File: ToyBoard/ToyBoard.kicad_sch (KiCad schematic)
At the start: 18 parts, among them J5 MSD-1-A, Q1 NMOS, Q2 NMOS

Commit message: Pcb and Gerbs for JLCPCB
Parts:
- removed LM66200DRLR1: ~, Package_TO_SOT_SMD:SOT-583-8, symbol NotinKi:LM66200DRLR
- added C2: C, Capacitor_SMD:C_0402_1005Metric_Pad0.74x0.62mm_HandSolder, symbol Device:C
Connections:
- net COVER_GND: now also C2.2
- net at C1.1, J5.4 (VDD), R1.1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: now also C2.1; no longer J5.3 (CMD), XiaoNRF1.5 (MISO)
- new net: J5.3 (CMD), XiaoNRF1.5 (MISO)
- no-connect marks 18 -> 15
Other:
- moved on the sheet: R1

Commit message: wiring rework
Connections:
- net at C1.1, C2.1, J5.4 (VDD)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: now also R1.2; no longer R1.1
- net at J5.2 (CD/DAT3), XiaoNRF1.4 (CS): now also R1.1; no longer R1.2
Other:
- moved on the sheet: R1
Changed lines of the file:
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@@
-	)
-	(junction
-		(at 134.62 135.89)
-		(diameter 0)
-		(color 0 0 0 0)
 	)
 	(junction
@@
 		(color 0 0 0 0)
 	)
+	(junction
+		(at 128.27 135.89)
+		(diameter 0)
+		(color 0 0 0 0)
+	)
 	(no_connect
 		(at 133.35 102.87)
@@
 	(wire
 		(pts
-			(xy 125.73 142.24) (xy 125.73 153.67)
+			(xy 125.73 142.24) (xy 125.73 143.51)
 		)
 		(stroke
@@
 	(wire
 		(pts
-			(xy 125.73 153.67) (xy 127 153.67)
+			(xy 128.27 135.89) (xy 148.59 135.89)
 		)
 		(stroke
@@
 	(wire
 		(pts
-			(xy 134.62 135.89) (xy 148.59 135.89)
-		)
-		(stroke
-			(width 0)
-			(type default)
-		)
-	)
-	(wire
-		(pts
 			(xy 127 87.63) (xy 125.73 87.63)
 		)
@@
 	(wire
 		(pts
+			(xy 128.27 151.13) (xy 128.27 135.89)
+		)
+		(stroke
+			(width 0)
+			(type default)
+		)
+	)
+	(wire
+		(pts
+			(xy 125.73 151.13) (xy 128.27 151.13)
+		)
+		(stroke
+			(width 0)
+			(type default)
+		)
+	)
+	(wire
+		(pts
 			(xy 109.22 69.85) (xy 96.52 69.85)
 		)
@@
 	(wire
 		(pts
-			(xy 128.27 135.89) (xy 134.62 135.89)
-		)
-		(stroke
-			(width 0)
-			(type default)
-		)
-	)
-	(wire
-		(pts
 			(xy 77.47 60.96) (xy 76.2 60.96)
 		)
@@
 		(pts
 			(xy 125.73 142.24) (xy 125.73 133.35)
-		)
-		(stroke
-			(width 0)
-			(type default)
-		)
-	)
-	(wire
-		(pts
-			(xy 134.62 135.89) (xy 134.62 153.67)
 		)
 		(stroke
@@
 		(on_board yes)
 		(dnp no)
-		(fields_autoplaced yes)
 		(property "Reference" "MAX98357"
-			(at 111.76 144.7799 90)
+			(at 88.646 140.97 0)
 			(effects
 				(font
@@
 		)
 		(property "Value" "~"
-			(at 111.76 147.3199 90)
+			(at 86.614 146.05 0)
 			(effects
 				(font
@@
 	(symbol
 		(lib_id "Device:R")
-		(at 130.81 153.67 270)
+		(at 125.73 147.32 0)
 		(unit 1)
 		(exclude_from_sim no)
@@
 		(dnp no)
 		(property "Reference" "R1"
-			(at 127 155.448 90)
+			(at 128.016 147.32 90)
 			(effects
 				(font
@@
 		)
 		(property "Value" "10k"
-			(at 129.794 156.464 90)
+			(at 123.444 147.32 90)
 			(effects
 				(font
@@
 		)
 		(property "Footprint" "Resistor_SMD:R_0805_2012Metric_Pad1.20x1.40mm_HandSolder"
-			(at 130.81 151.892 90)
+			(at 123.952 147.32 90)
 			(effects
 				(font
@@
 		)
 		(property "Datasheet" "~"
-			(at 130.81 153.67 0)
+			(at 125.73 147.32 0)
 			(effects
 				(font
@@
 		)
 		(property "Description" "Resistor"
-			(at 130.81 153.67 0)
-			(effects
-				(font
+			(at 125.73 147.32 0)
+			(effects
+				(font

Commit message: cleared schem
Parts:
- renumbered U1 to LiPo_charger1
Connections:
- net pwm_out1: now reaches Q1.2 (G), R3.1, XiaoNRF1.8 (PWM1)
- net pwm_out2: now reaches Q2.2 (G), R4.1, XiaoNRF1.10 (PWM2)
- net max_din: now reaches MAX98357.5 (DIN), XiaoNRF1.11 (D4)
- net max_bclk: now reaches MAX98357.6 (BCLK), XiaoNRF1.12 (D5)
- net max_lrc: now reaches MAX98357.7 (LRC), XiaoNRF1.13 (D6)
- net 3V3: now reaches C1.1, C2.1, J5.4 (VDD), R1.2, XiaoNRF1.3 (3V3)
- net sd_cs: now reaches J5.2 (CD/DAT3), R1.1, XiaoNRF1.4 (CS)
- net sd_mosi: now reaches J5.3 (CMD), XiaoNRF1.5 (MOSI)
- net sd_sck: now reaches J5.5 (CLK), XiaoNRF1.6 (SCK)
- net sd_miso: now reaches J5.7 (DAT0), XiaoNRF1.7 (MISO)
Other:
- moved on the sheet: C1, C2, D1, D2, D3, J1, J2, J3, MAX98357, Q1, Q2, R3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

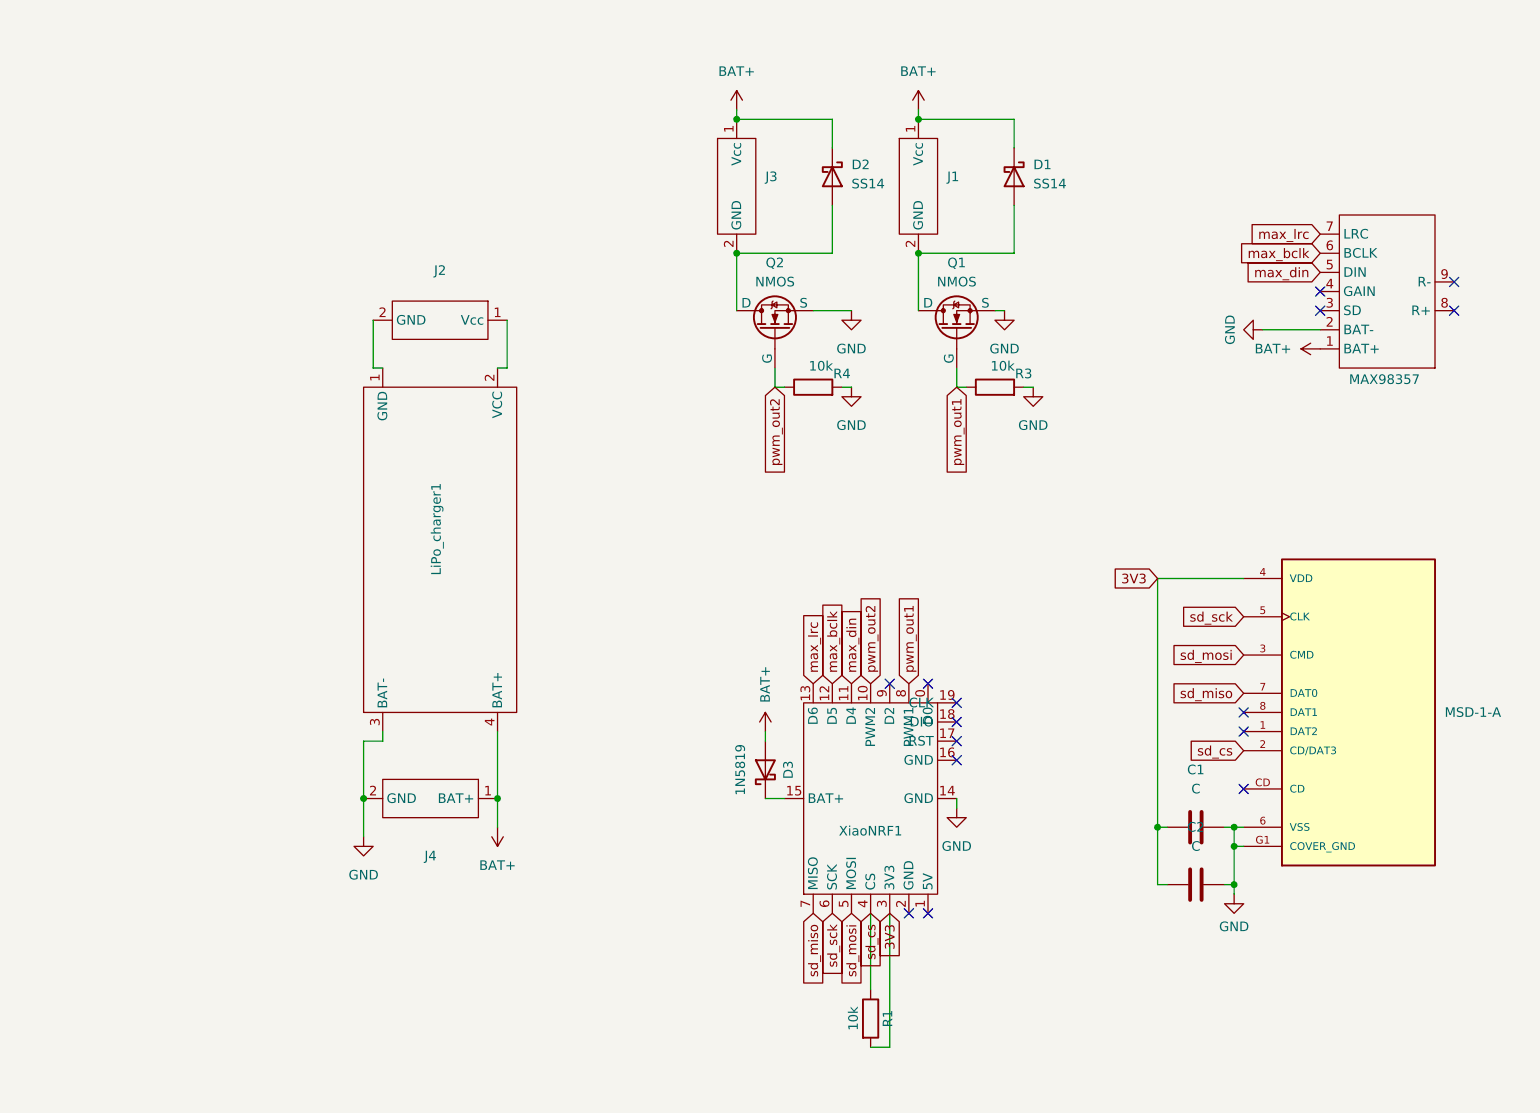
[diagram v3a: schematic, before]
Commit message: cleaner schematic
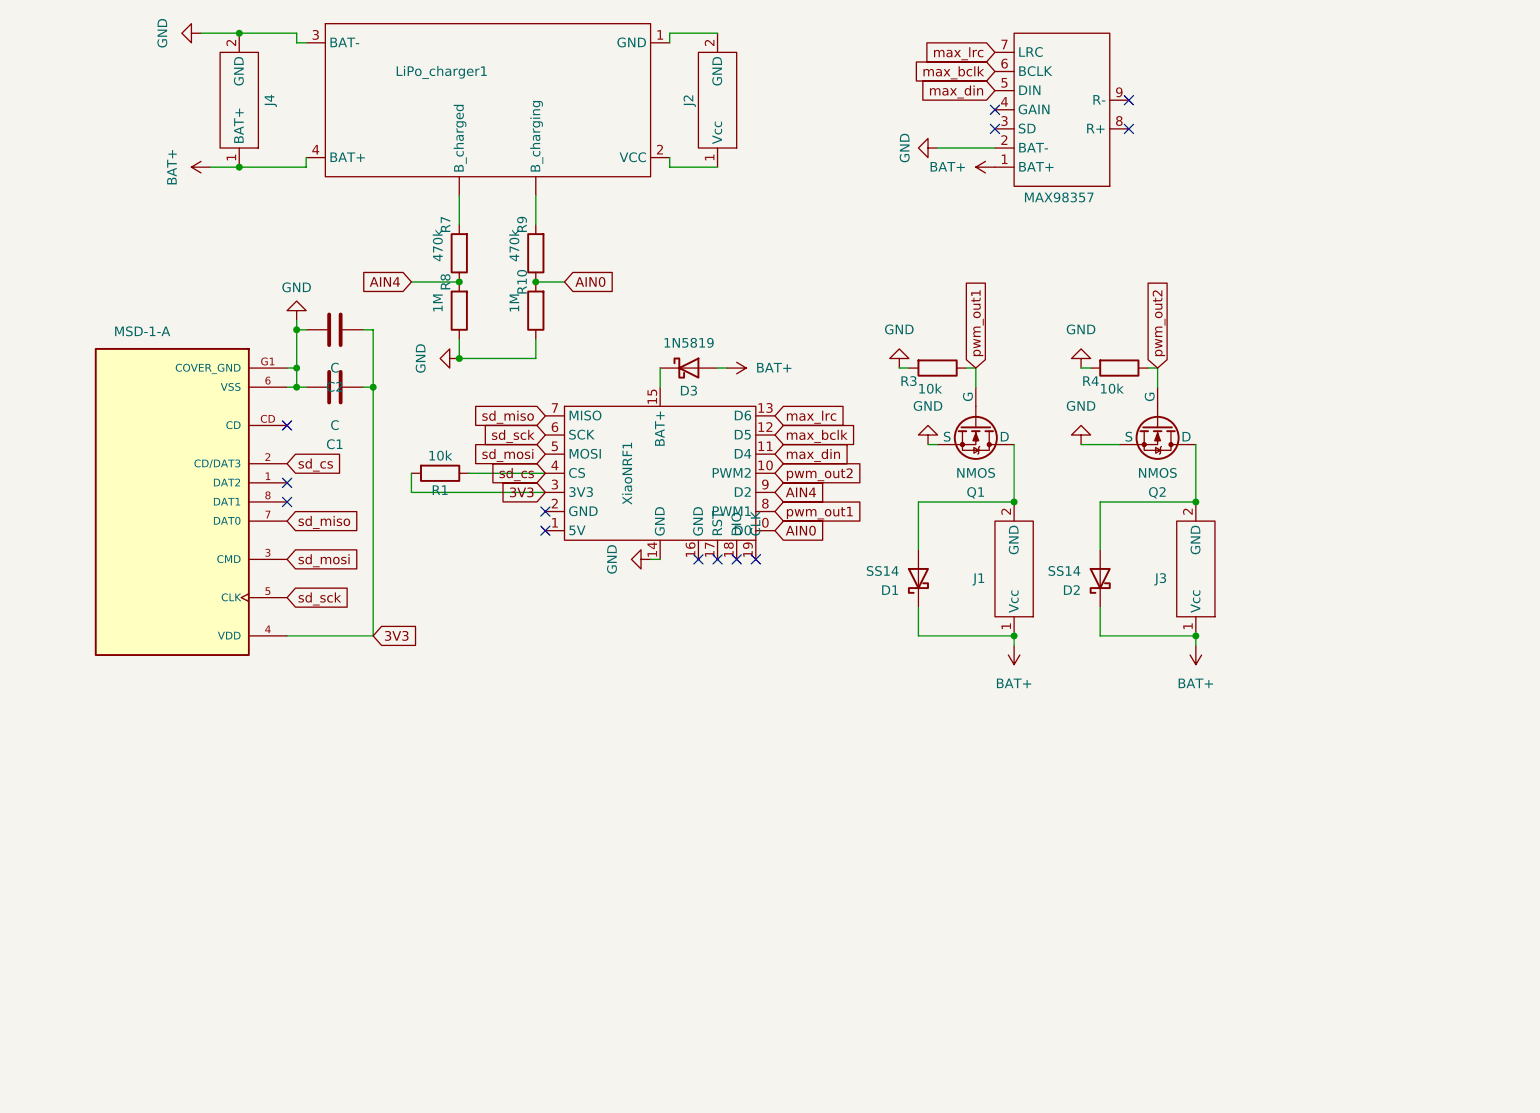
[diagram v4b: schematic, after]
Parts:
- added R10, R8: 1M, Resistor_SMD:R_0805_2012Metric_Pad1.20x1.40mm_HandSolder, symbol Device:R
- added R7, R9: 470k, Resistor_SMD:R_0805_2012Metric_Pad1.20x1.40mm_HandSolder, symbol Device:R
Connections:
- net COVER_GND: now also R10.1, R8.1
- net AIN0: now reaches XiaoNRF1.0 (D0)
- net AIN0: now also R10.2, R9.1
- net AIN4: now reaches XiaoNRF1.9 (D2)
- net AIN4: now also R7.1, R8.2
- new net: LiPo_charger1. (B_charging), R9.2
- new net: LiPo_charger1. (B_charging), R7.2
- no-connect marks 15 -> 13
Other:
- moved on the sheet: C1, C2, D1, D2, D3, J1, J2, J3, J4, MAX98357, Q1, Q2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
